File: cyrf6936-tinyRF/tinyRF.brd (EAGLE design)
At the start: 13 x 13 mm, 23 parts

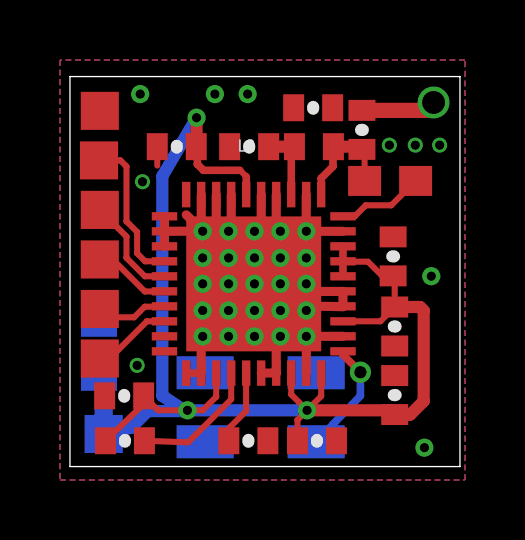
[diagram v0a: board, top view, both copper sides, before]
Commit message: Screwed up that last commit.  this update include changes to the production gerber folders.  Adds hackvana to the cyrf6936-BoB and cleans up the fab notes a bit.  Still need to standardize and parameterize the creation of the gerbers.
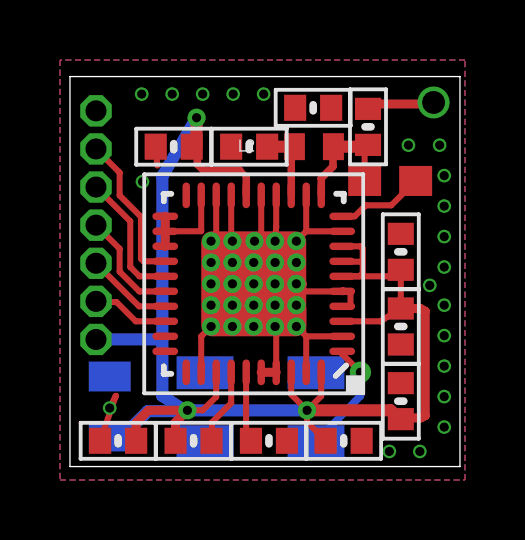
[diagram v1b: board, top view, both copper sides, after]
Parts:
- removed _SS: SOLDER_PAD.05X.05, JCM:SOLDER_PAD_.05X.05
- added !SS: SOLDER_PADTH, JCM-Connectors:1X1_50MIL
- C1, C10, C11, C15, C3, C4, C5, C6, C7, C8, C9: device SparkFun-Passives:0402-CAP -> JCM-Capacitors:0402-CAP
- C14: device SparkFun-Passives:0805 -> JCM-Capacitors:0805
- CYRF6936: value CYRF6936 -> CYRF6936QFN; device JCM:QFN40 -> JCM-IC:QFN50P600X600X90-41N
- GND, IRQ, MISO, MOSI, SCK, VCC: value SOLDER_PAD.05X.05 -> SOLDER_PADTH; device JCM:SOLDER_PAD_.05X.05 -> JCM-Connectors:1X1_50MIL
- moved VCC 3.16 mm to (12.7, 19.7)
- moved C15 2.29 mm to (16.0, 16.3)
- moved MISO 1.91 mm to (12.7, 21.0)
- moved C14 1.86 mm to (13.2, 17.4)
- moved MOSI 1.53 mm to (12.7, 22.2)
- moved C8 1.51 mm to (13.4, 16.3)
- moved IRQ 1.15 mm to (12.7, 23.5)
- moved C9 0.89 mm to (21.0, 16.3)
- moved SCK 0.77 mm to (12.7, 24.8)
- moved C5 0.69 mm to (18.5, 16.3)
- moved C11 0.30 mm to (22.9, 22.6)
- moved C7 0.29 mm to (22.9, 17.6)
- moved C1 0.23 mm to (21.8, 26.8)
- moved C10 0.20 mm to (22.9, 20.1)
- moved GND 0.13 mm to (12.7, 27.3)
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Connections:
- net GND: now also CYRF6936.41, GND.1; no longer CYRF6936.GND, GND.P$1
- net IRQ: now also IRQ.1; no longer IRQ.P$1
- net MISO: now also MISO.1; no longer MISO.P$1
- net MOSI: now also MOSI.1; no longer MOSI.P$1
- net SCK: now also SCK.1; no longer SCK.P$1
- net VCC: now also VCC.1; no longer VCC.P$1
- net _SS: now also !SS.1; no longer _SS.P$1
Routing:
- net VCC: track 47.6 -> 50.8 mm
- net RST: track 4.36 -> 2.55 mm
- net GND: track 32.9 -> 34.3 mm, vias 35 -> 46
- net IRQ: track 2.60 -> 3.67 mm
- net SCK: track 3.49 -> 4.43 mm
- net MOSI: track 2.42 -> 2.94 mm
